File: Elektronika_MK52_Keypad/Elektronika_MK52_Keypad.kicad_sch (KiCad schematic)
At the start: 33 parts, among them J1 Keypad PCB, SW1 F, SW10 ШГ←, SW11 Х←П, SW12 4, SW13 5, SW14 6, SW15 +, SW16 *, SW17 ↓↑, SW18 B/O, SW19 БП, SW2 ШГ→, SW20 1, SW21 2, SW22 3, SW23 ↔, SW24 В↑, SW25 A↑, SW26 С/П, SW27 ПП, SW28 0, SW29 ., SW3 П→Х, SW30 /-/, SW31 ВП, SW32 СХ, SW4 7, SW5 8, SW6 9, SW7 -, SW8 ÷, SW9 K

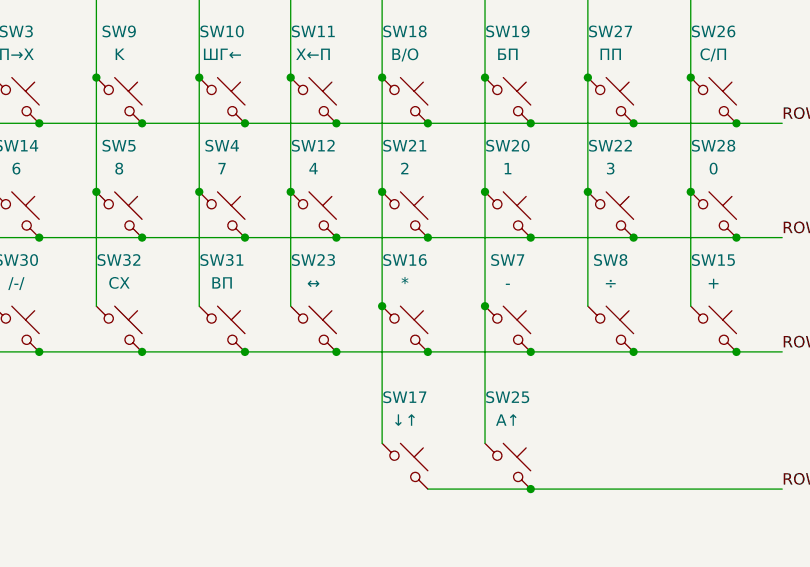
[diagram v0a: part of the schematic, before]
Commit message: Created PCB outline
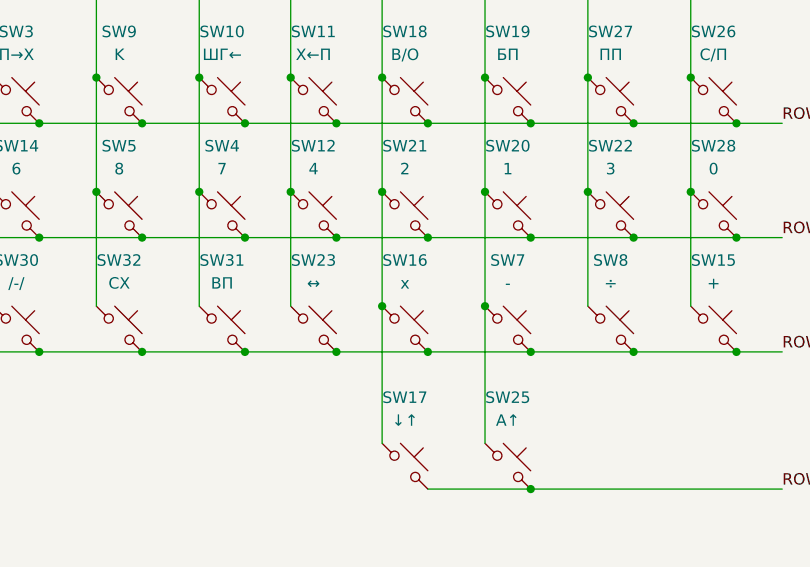
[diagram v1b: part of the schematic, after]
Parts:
- SW16: value * -> x
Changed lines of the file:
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@@
 			)
 		)
-		(property "Value" "*"
+		(property "Value" "x"
 			(at 125.73 100.33 0)
 			(effects

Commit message: initial PCB routing
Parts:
- J1: footprint Connector_PinHeader_1.00mm:PinHeader_1x14_P1.00mm_Vertical_SMD_Pin1Right -> Connector_PinHeader_1.00mm:PinHeader_1x14_P1.00mm_Vertical
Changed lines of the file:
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@@
 			)
 		)
-		(property "Footprint" "Connector_PinHeader_1.00mm:PinHeader_1x14_P1.00mm_Vertical_SMD_Pin1Right"
+		(property "Footprint" "Connector_PinHeader_1.00mm:PinHeader_1x14_P1.00mm_Vertical"
 			(at 220.98 93.98 0)
 			(effects

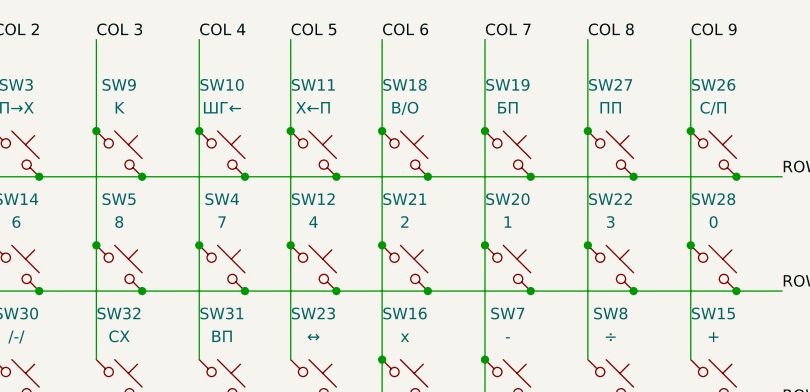
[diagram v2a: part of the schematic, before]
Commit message: Revised PCB layout
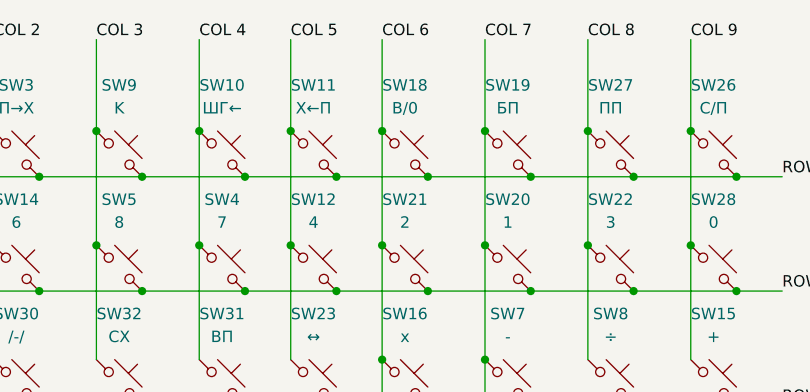
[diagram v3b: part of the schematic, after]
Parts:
- SW18: value B/O -> B/0
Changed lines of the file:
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@@
 			)
 		)
-		(property "Value" "B/O"
+		(property "Value" "B/0"
 			(at 125.73 74.93 0)
 			(effects
